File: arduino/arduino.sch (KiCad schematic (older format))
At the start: 2 parts

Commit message: main circuit in place
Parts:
- added C? (x3): C, ~, symbol C
- added C?: CP1, ~, symbol CP1
- added P?: CONN_1, symbol CONN_1
- added P?: CONN_6, symbol CONN_6
- added P?: CONN_2, symbol CONN_2
- added Q?: CSTLS_X, murata-resonators-CSTLS_X, symbol CSTLS_X
- added R?: R, ~, symbol R
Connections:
- net GND: now also U?.7 (GND), C?.2, C?.2, C?.2, P?.1, Q?.2 (VSS)
- net VCC: now also IC?.20 (AVCC), C?.1, C?.1, P?.1 (P1), R?.1
- net at IC?.1 ((PCINT14/~RESET~)PC6): now also C?.1, R?.2
- net at IC?.10 ((PCINT7/XTAL2/TOSC2)PB7): now also Q?.1
- net at IC?.2 ((PCINT16/RXD)PD0): now also P?.4
- net at IC?.21 (AREF): now also C?.1
- net at IC?.3 ((PCINT17/TXD)PD1): now also P?.5
- net at IC?.9 ((PCINT6/XTAL1/TOSC1)PB6): now also Q?.3
- net at U?.8 (ANT): now also P?.1
- new net: P?.2 (PM), P?.3
- new net: C?.2, P?.6
- no-connect marks 0 -> 6

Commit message: wip
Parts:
- added P3, P4: CONN_6, symbol CONN_6
- C2, C4: renamed from C?; value C -> 0.1u
- C3: renamed from C?; value CP1 -> 10u
- Q1: renamed from Q?; value CSTLS_X -> 16MHz
- R1: renamed from R?; value R -> 10k
- gave numbers to parts that had none: 6
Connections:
- net GND: now also P3.3, P4.3
- net VCC: now also P3.1, P3.4, P4.1, P4.4
- net at IC1.11 ((PCINT21/OC0B/T1)PD5): now also P4.2
- net at IC1.23 ((PCINT8/ADC0)PC0): now also P3.5
- net at IC1.24 ((PCINT9/ADC1)PC1): now also P4.5
- net at IC1.5 ((PCINT19/OC2B/INT1)PD3): now also P3.6, P4.6
- net at IC1.6 ((PCINT20/XCK/T0)PD4): now also P3.2
- no-connect marks 6 -> 14
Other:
- moved on the sheet: C2, C3, C4, Q1

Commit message: first valid layout - added connector
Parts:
- added P6: CONN_6, symbol CONN_6
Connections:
- net GND: now also P6.6
- net at IC1.12 ((PCINT22/OC0A/AIN0)PD6): now also P6.4
- net at IC1.13 ((PCINT23/AIN1)PD7): now also P6.3
- net at IC1.14 ((PCINT0/CLKO/ICP1)PB0): now also P6.2
- net at IC1.16 ((PCINT2/OC1B/~SS~)PB2): now also P6.1
- no-connect marks 14 -> 11
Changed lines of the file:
@@
 NoConn ~ 3800 2900
 NoConn ~ 3800 3000
-NoConn ~ 3800 1850
-NoConn ~ 3800 1650
-NoConn ~ 3800 3850
-NoConn ~ 3800 3950
 $Comp
 L PWR_FLAG #FLG015
@@
 	1500 1750 1700 1750
 Connection ~ 1700 1750
+$Comp
+L CONN_6 P6
+U 1 1 55A3BFD5
+P 5750 1250
+F 0 "P6" V 5700 1250 60  0000 C CNN
+F 1 "CONN_6" V 5800 1250 60  0000 C CNN
+F 2 "" H 5750 1250 60  0000 C CNN
+F 3 "" H 5750 1250 60  0000 C CNN
+	1    5750 1250
+	1    0    0    -1
+$EndComp
+Wire Wire Line
+	3800 1650 5000 1650
+Wire Wire Line
+	5050 1850 3800 1850
+Wire Wire Line
+	5050 1000 5050 1850
+Wire Wire Line
+	3800 3850 3850 3850
+Wire Wire Line
+	3850 3850 3850 2700
+Wire Wire Line
+	3850 2700 4200 2700
+Wire Wire Line
+	4200 2700 4200 2200
+Wire Wire Line
+	4200 2200 5150 2200
+Wire Wire Line
+	3800 3950 3900 3950
+Wire Wire Line
+	3900 3950 3900 2800
+Wire Wire Line
+	3900 2800 4250 2800
+Wire Wire Line
+	4250 2800 4250 2300
+Wire Wire Line
+	4250 2300 5200 2300
+Wire Wire Line
+	5200 2300 5200 1200
+$Comp
+L GND #PWR019
+U 1 1 55A3C1C6
+P 5300 1600
+F 0 "#PWR019" H 5300 1600 30  0001 C CNN
+F 1 "GND" H 5300 1530 30  0001 C CNN
+F 2 "" H 5300 1600 60  0000 C CNN
+F 3 "" H 5300 1600 60  0000 C CNN
+	1    5300 1600
+	1    0    0    -1
+$EndComp
+Wire Wire Line
+	5300 1600 5300 1500
+Wire Wire Line
+	5300 1500 5400 1500
+NoConn ~ 5400 1400
+Wire Wire Line
+	5050 1000 5400 1000
+Wire Wire Line
+	5000 1100 5400 1100
+Wire Wire Line
+	5400 1100 5400 1150
+Wire Wire Line
+	5000 1650 5000 1100
+Wire Wire Line
+	5200 1200 5400 1200
+Wire Wire Line
+	5150 1300 5400 1300
+Wire Wire Line
+	5150 2200 5150 1300
 $EndSCHEMATC

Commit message: more pcb work
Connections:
- net VCC: now also P6.5
- no-connect marks 11 -> 10
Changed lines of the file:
@@
 Wire Wire Line
 	5300 1500 5400 1500
-NoConn ~ 5400 1400
 Wire Wire Line
 	5050 1000 5400 1000
@@
 Wire Wire Line
 	5150 2200 5150 1300
+Wire Wire Line
+	5400 1400 4950 1400
+Wire Wire Line
+	4950 1400 4950 1000
+Wire Wire Line
+	4950 1000 4800 1000
+Connection ~ 4800 1000
 $EndSCHEMATC

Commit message: wip
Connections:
- net VCC: now also R1.2; no longer R1.1
- net at C4.1, IC1.1 ((PCINT14/~RESET~)PC6): now also R1.1; no longer R1.2
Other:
- moved on the sheet: R1
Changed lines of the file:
@@
 Sheet 1 1
 Title ""
-Date "13 jul 2015"
+Date "14 jul 2015"
 Rev ""
 Comp ""
@@
 L R R1
 U 1 1 55A3972A
-P 4800 1350
-F 0 "R1" V 4880 1350 40  0000 C CNN
-F 1 "10k" V 4807 1351 40  0000 C CNN
-F 2 "~" V 4730 1350 30  0000 C CNN
-F 3 "~" H 4800 1350 30  0000 C CNN
-	1    4800 1350
-	1    0    0    -1
+P 5050 2450
+F 0 "R1" V 5130 2450 40  0000 C CNN
+F 1 "10k" V 5057 2451 40  0000 C CNN
+F 2 "~" V 4980 2450 30  0000 C CNN
+F 3 "~" H 5050 2450 30  0000 C CNN
+	1    5050 2450
+	0    -1   -1   0
 $EndComp
 Wire Wire Line
@@
 L VCC #PWR04
 U 1 1 55A39778
-P 4800 950
-F 0 "#PWR04" H 4800 1050 30  0001 C CNN
-F 1 "VCC" H 4800 1050 30  0000 C CNN
-F 2 "" H 4800 950 60  0000 C CNN
-F 3 "" H 4800 950 60  0000 C CNN
-	1    4800 950
-	1    0    0    -1
+P 5450 2450
+F 0 "#PWR04" H 5450 2550 30  0001 C CNN
+F 1 "VCC" H 5450 2550 30  0000 C CNN
+F 2 "" H 5450 2450 60  0000 C CNN
+F 3 "" H 5450 2450 60  0000 C CNN
+	1    5450 2450
+	0    1    1    0
 $EndComp
 $Comp
@@
 	-1   0    0    1
 $EndComp
-Wire Wire Line
-	4800 950  4800 1100
-Wire Wire Line
-	4800 1600 4650 1600
-Wire Wire Line
-	4650 1600 4650 3100
 $Comp
 L GND #PWR05
@@
 Wire Wire Line
 	4950 1000 4800 1000
-Connection ~ 4800 1000
+Wire Wire Line
+	4800 2450 4650 2450
+Wire Wire Line
+	5300 2450 5450 2450
+Wire Wire Line
+	4650 2450 4650 3100
+$Comp
+L VCC #PWR?
+U 1 1 55A5274D
+P 4800 950
+F 0 "#PWR?" H 4800 1050 30  0001 C CNN
+F 1 "VCC" H 4800 1050 30  0000 C CNN
+F 2 "" H 4800 950 60  0000 C CNN
+F 3 "" H 4800 950 60  0000 C CNN
+	1    4800 950
+	1    0    0    -1
+$EndComp
+Wire Wire Line
+	4800 1000 4800 950
 $EndSCHEMATC

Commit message: add battery connector
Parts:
- added P7: CONN_2, symbol CONN_2
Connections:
- net GND: now also P7.1 (P1)
- net VCC: now also P7.2 (PM)
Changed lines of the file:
@@
 	2450 4350 2450 4300
 Wire Wire Line
-	2450 4300 2750 4300
+	2250 4300 2750 4300
 Wire Wire Line
 	2750 4300 2750 4350
@@
 	2450 4750 2450 4800
 Wire Wire Line
-	2450 4800 2750 4800
+	2250 4800 2750 4800
 Wire Wire Line
 	2750 4800 2750 4750
@@
 	4650 2450 4650 3100
 $Comp
-L VCC #PWR?
+L VCC #PWR020
 U 1 1 55A5274D
 P 4800 950
-F 0 "#PWR?" H 4800 1050 30  0001 C CNN
+F 0 "#PWR020" H 4800 1050 30  0001 C CNN
 F 1 "VCC" H 4800 1050 30  0000 C CNN
 F 2 "" H 4800 950 60  0000 C CNN
@@
 Wire Wire Line
 	4800 1000 4800 950
+$Comp
+L CONN_2 P7
+U 1 1 55A57212
+P 1900 4550
+F 0 "P7" V 1850 4550 40  0000 C CNN
+F 1 "CONN_2" V 1950 4550 40  0000 C CNN
+F 2 "" H 1900 4550 60  0000 C CNN
+F 3 "" H 1900 4550 60  0000 C CNN
+	1    1900 4550
+	-1   0    0    1
+$EndComp
+Wire Wire Line
+	2250 4450 2250 4300
+Connection ~ 2450 4300
+Wire Wire Line
+	2250 4650 2250 4800
+Connection ~ 2450 4800
 $EndSCHEMATC

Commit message: pcb text
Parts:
- P7: value CONN_2 -> battery
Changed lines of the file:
@@
 P 1900 4550
 F 0 "P7" V 1850 4550 40  0000 C CNN
-F 1 "CONN_2" V 1950 4550 40  0000 C CNN
+F 1 "battery" V 1950 4550 40  0000 C CNN
 F 2 "" H 1900 4550 60  0000 C CNN
 F 3 "" H 1900 4550 60  0000 C CNN

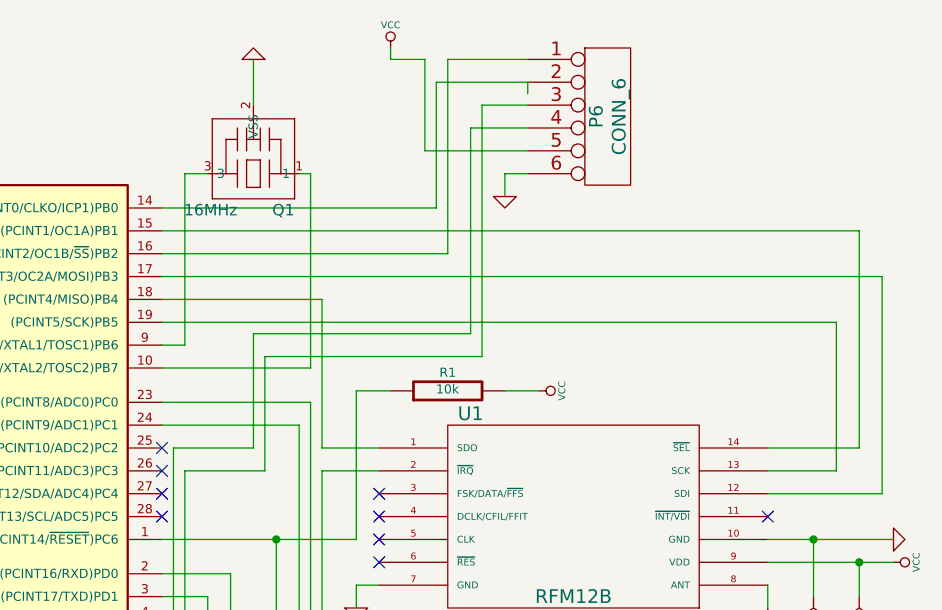
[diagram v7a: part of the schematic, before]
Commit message: swap pins 15/16 on cpu
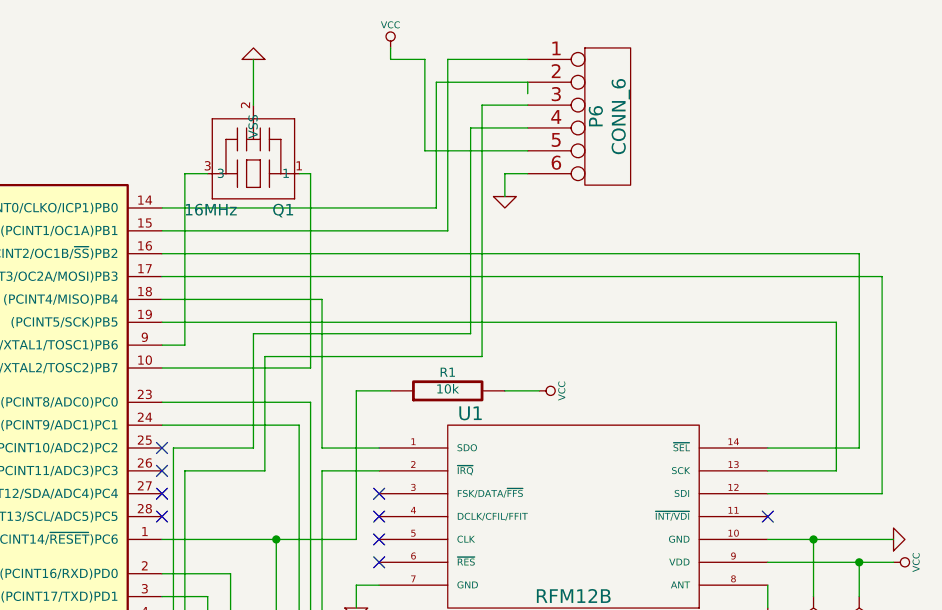
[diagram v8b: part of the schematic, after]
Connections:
- net at IC1.15 ((PCINT1/OC1A)PB1): now also P6.1; no longer U1.14 (~SEL)
- net at IC1.16 ((PCINT2/OC1B/~SS~)PB2): now also U1.14 (~SEL); no longer P6.1
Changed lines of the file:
@@
 Sheet 1 1
 Title ""
-Date "14 jul 2015"
+Date "15 jul 2015"
 Rev ""
 Comp ""
@@
 $EndComp
 Wire Wire Line
-	3800 1750 6850 1750
-Wire Wire Line
-	6850 1750 6850 2700
-Wire Wire Line
 	6850 2700 6450 2700
 Wire Wire Line
@@
 	3800 1650 5000 1650
 Wire Wire Line
-	5050 1850 3800 1850
-Wire Wire Line
-	5050 1000 5050 1850
-Wire Wire Line
 	3800 3850 3850 3850
 Wire Wire Line
@@
 	2250 4650 2250 4800
 Connection ~ 2450 4800
+Wire Wire Line
+	3800 1750 5050 1750
+Wire Wire Line
+	5050 1750 5050 1000
+Wire Wire Line
+	3800 1850 6850 1850
+Wire Wire Line
+	6850 1850 6850 2700
 $EndSCHEMATC
